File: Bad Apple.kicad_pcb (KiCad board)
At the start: 4 copper layers, 65 x 56 mm, 29 parts, among them J1 GPIO, J10 Conn_01x04, J16 Conn_02x03_Counter_Clockwise, J17 Conn_02x03_Counter_Clockwise, J2 Conn_01x02, J3 Conn_01x02, J4 Conn_01x02, J5 Conn_01x02, J6 Conn_01x02, J7 Conn_01x04, J8 Conn_01x02, J9 Conn_01x04, Q1 SS8050, U1 CAT24C256, U2 ICM-20948, U3 TXS0104EPW, U5 TB6612FNG, U6 TB6612FNG, U7 MAX98357A

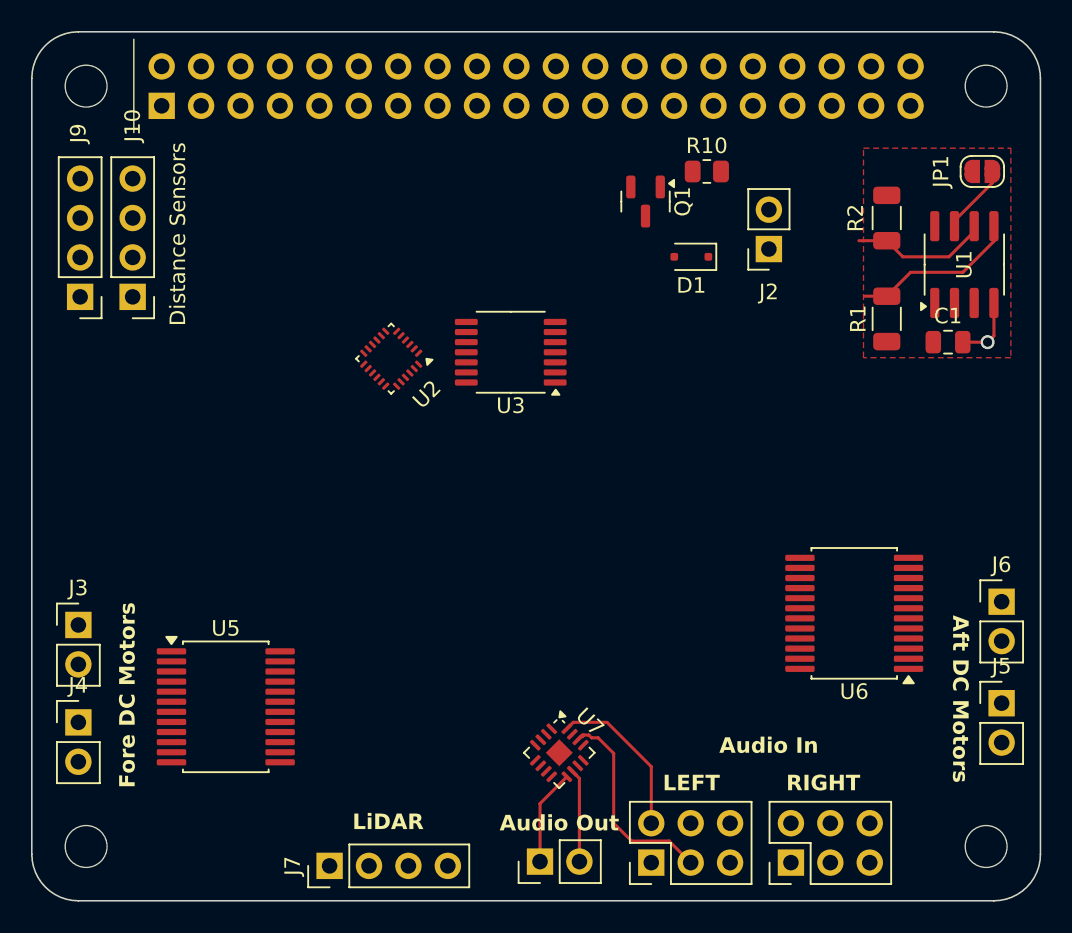
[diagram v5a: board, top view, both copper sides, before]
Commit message: feat(pcb): L1 +5V ground pour
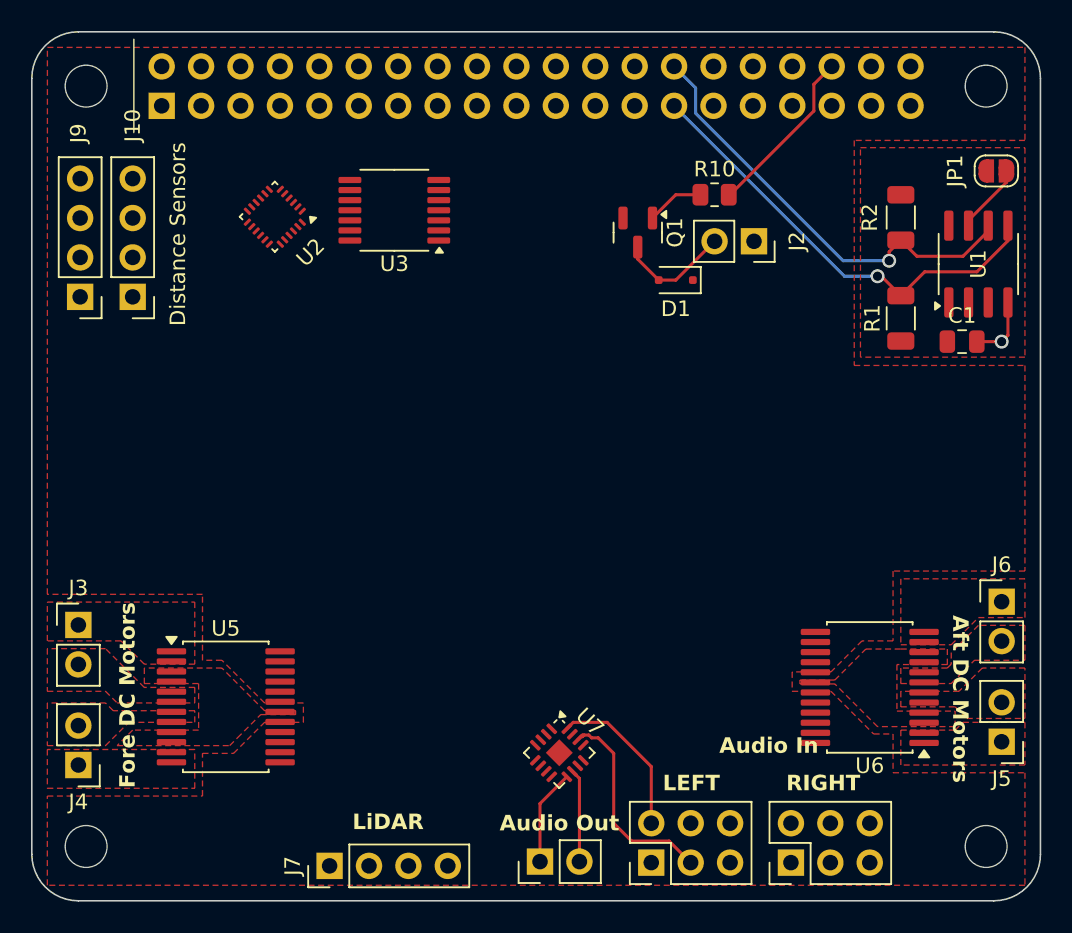
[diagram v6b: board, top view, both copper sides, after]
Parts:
- moved U3 11.8 mm to (123.4, 55.5)
- moved U2 11.8 mm to (115.7, 55.9)
- moved U6 4.88 mm to (154.0, 86.2)
- moved J4 2.75 mm to (103.0, 91.2), turned to 180 degrees
- moved J5 2.48 mm to (162.5, 89.8), turned to 180 degrees
- moved Q1 2.06 mm to (139.1, 56.9)
- moved D1 1.80 mm to (141.5, 60.0)
- moved R10 1.58 mm to (144.0, 54.5)
- moved J2 1.08 mm to (146.5, 57.5), turned to -90 degrees
- moved JP1 0.91 mm to (162.2, 53.0)
- moved R1 0.91 mm to (156.0, 62.5)
- moved R2 0.91 mm to (156.0, 56.0)
- moved U1 0.91 mm to (161.0, 59.0)
- moved C1 0.91 mm to (159.9, 64.0)
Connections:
- U5 pad 10: Net-(U5-PGND2-Pad10) -> GND
- U5 pad 13: unconnected-(U5-VM2-Pad13) -> +12V
- U5 pad 14: unconnected-(U5-VM3-Pad14) -> +12V
- U5 pad 18: unconnected-(U5-GND-Pad18) -> GND
- U5 pad 20: unconnected-(U5-VCC-Pad20) -> +5V
- U5 pad 24: unconnected-(U5-VM1-Pad24) -> +12V
- U5 pad 3: Net-(U5-PGND1-Pad3) -> GND
- U5 pad 4: Net-(U5-PGND1-Pad3) -> GND
- U5 pad 9: Net-(U5-PGND2-Pad10) -> GND
- U6 pad 10: Net-(U6-PGND2-Pad10) -> GND
- U6 pad 13: unconnected-(U6-VM2-Pad13) -> +12V
- U6 pad 14: unconnected-(U6-VM3-Pad14) -> +12V
- U6 pad 18: unconnected-(U6-GND-Pad18) -> GND
- U6 pad 20: unconnected-(U6-VCC-Pad20) -> +5V
- U6 pad 24: unconnected-(U6-VM1-Pad24) -> +12V
- U6 pad 3: Net-(U6-PGND1-Pad3) -> GND
- U6 pad 4: Net-(U6-PGND1-Pad3) -> GND
- U6 pad 9: Net-(U6-PGND2-Pad10) -> GND
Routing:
- net /[1] HAT Interface/ID_SCL: track 8.88 -> 28.7 mm, vias 0 -> 1
- net /[1] HAT Interface/ID_SDA: track 10.8 -> 29.0 mm, vias 0 -> 1
- net /[1] HAT Interface/GPIO16: track 0.00 -> 11.1 mm
- net Net-(D1-A): track 0.00 -> 7.32 mm
- net Net-(Q1-B): track 0.00 -> 3.71 mm
- added copper zone on F.Cu, net +5V
- added copper zone on F.Cu, net /[4] Motors/MOTOR A1
- added copper zone on F.Cu, net /[4] Motors/MOTOR A2
- added copper zone on F.Cu, net /[4] Motors/MOTOR B1
- added copper zone on F.Cu, net /[4] Motors/MOTOR B2
- added copper zone on F.Cu, net /[4] Motors/MOTOR C1
- added copper zone on F.Cu, net /[4] Motors/MOTOR C2
- added copper zone on F.Cu, net /[4] Motors/MOTOR D1
- added copper zone on F.Cu, net /[4] Motors/MOTOR D2
- added copper zone on F.Cu, net GND

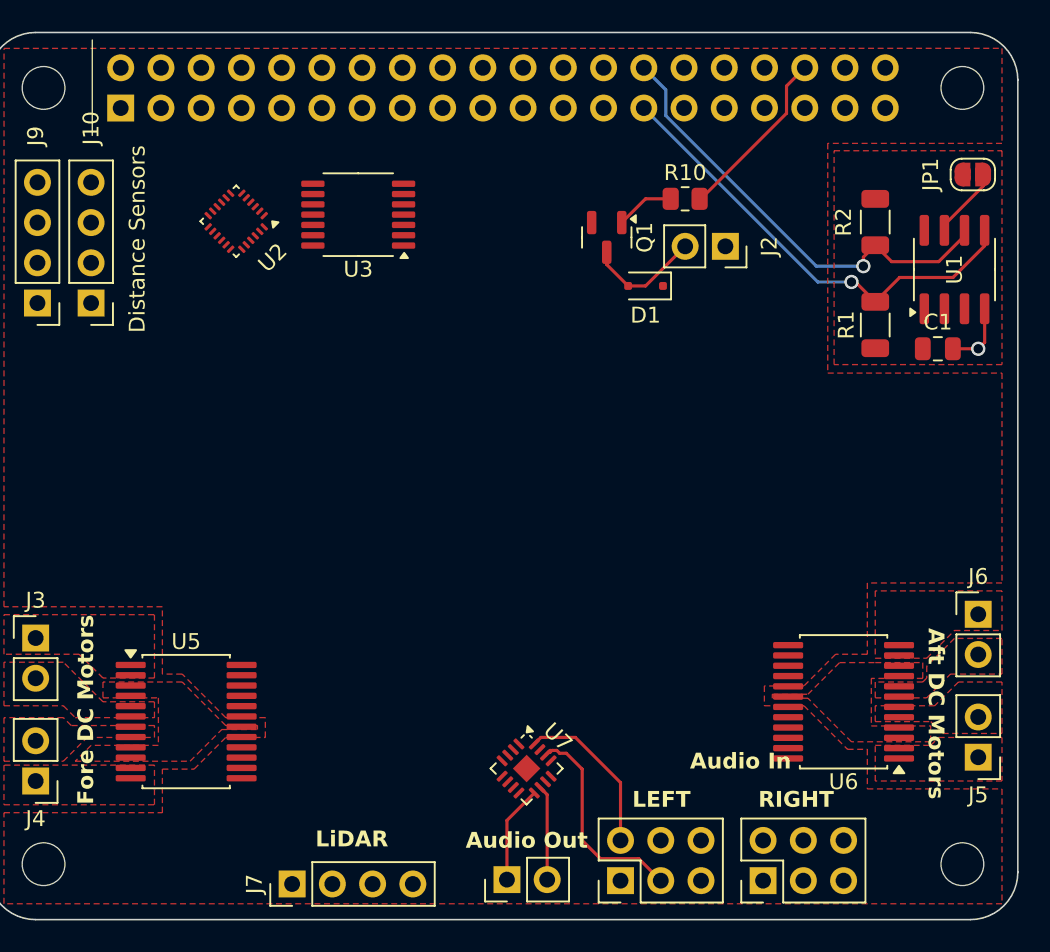
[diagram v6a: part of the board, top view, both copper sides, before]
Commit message: feat: wired up audio system
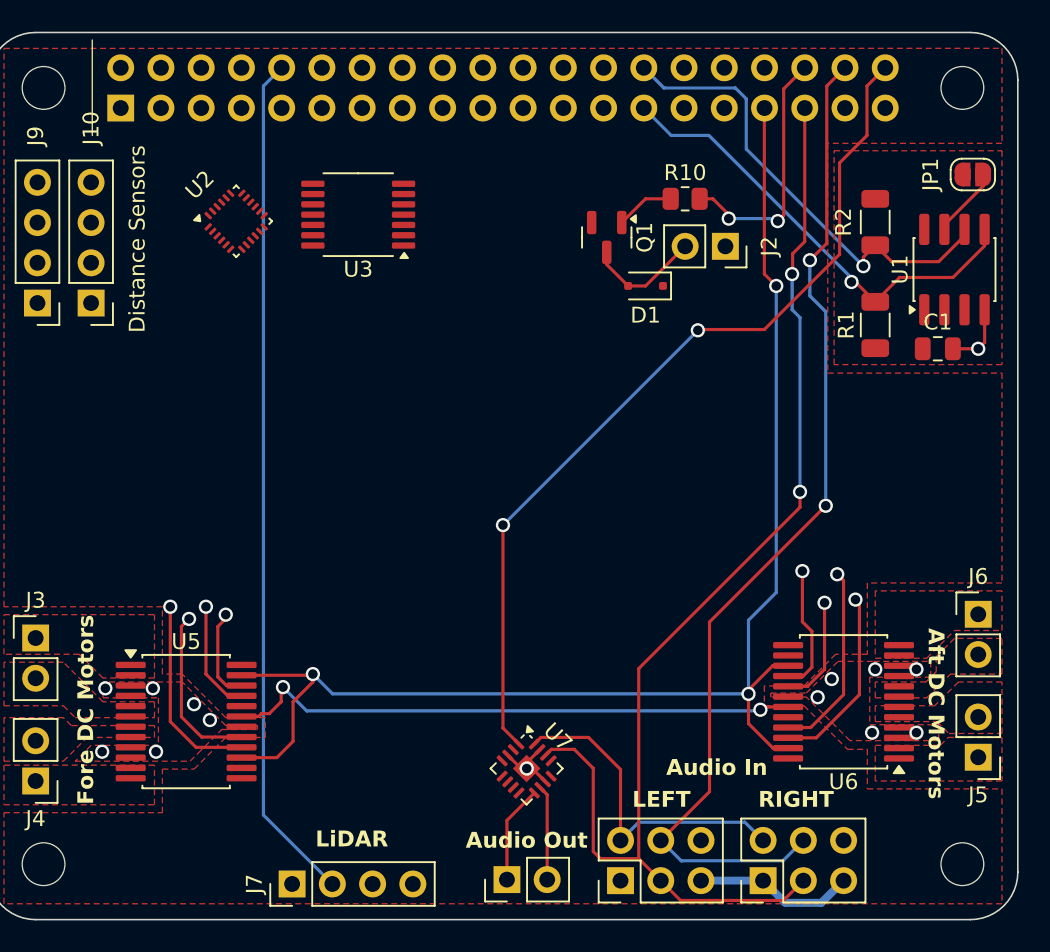
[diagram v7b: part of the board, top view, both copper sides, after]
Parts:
- U1: footprint Package_SO:SOIC-8_3.9x4.9mm_P1.27mm -> Package_SO:SOP-8_3.76x4.96mm_P1.27mm
- turned U2 to 45 degrees
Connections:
- U6 pad 16: /[1] HAT Interface/GPIO6 -> /[4] Motors/M4DB
- U6 pad 17: /[1] HAT Interface/GPIO5 -> /[4] Motors/M4DA
- U6 pad 21: /[1] HAT Interface/GPIO17 -> /[4] Motors/M3DA
- U6 pad 22: /[1] HAT Interface/GPIO27 -> /[4] Motors/M3DB
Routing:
- net /[1] HAT Interface/GPIO13/PWM1: track 0.00 -> 87.4 mm, vias 0 -> 3
- net /[1] HAT Interface/GPIO20/PCM.DIN: track 0.00 -> 64.6 mm, vias 0 -> 2
- net /[1] HAT Interface/GPIO19/PCM.FS: track 13.6 -> 76.1 mm, vias 0 -> 2
- net /[1] HAT Interface/GPIO21/PCM.DOUT: track 0.00 -> 55.5 mm, vias 0 -> 2
- net /[1] HAT Interface/GPIO15/RXD0: track 0.00 -> 53.8 mm
- net /[1] HAT Interface/GPIO26: track 0.00 -> 36.5 mm, vias 0 -> 2
- net /[1] HAT Interface/GPIO6: track 0.00 -> 12.4 mm, vias 0 -> 1
- net /[4] Motors/M3DA: track 0.00 -> 12.3 mm, vias 0 -> 1
- net /[4] Motors/M3DB: track 0.00 -> 11.7 mm, vias 0 -> 1
- net /[1] HAT Interface/GPIO5: track 0.00 -> 10.7 mm, vias 0 -> 1
- net /[1] HAT Interface/GPIO18/PCM.CLK: track 10.4 -> 20.9 mm
- net +3.3V: track 0.00 -> 10.2 mm
- net /[4] Motors/M4DB: track 0.00 -> 8.05 mm, vias 0 -> 1
- net /[1] HAT Interface/GPIO17: track 0.00 -> 7.07 mm, vias 0 -> 1
- net /[4] Motors/M4DA: track 0.00 -> 6.95 mm, vias 0 -> 1
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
